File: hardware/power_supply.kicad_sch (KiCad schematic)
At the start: 45 parts

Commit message: schematic
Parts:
- removed C210, C?: (no value), symbol tinkerforge:CP1
- removed C? (x9): (no value), symbol tinkerforge:C
- removed D?: (no value), symbol tinkerforge:DIODESCH
- removed R? (x4): (no value), symbol tinkerforge:R
- removed U?: (no value), symbol tinkerforge:BD906XX-C-HRP7
- added C?: 100nF, kicad-libraries:C0603F, symbol tinkerforge:C
- added C? (x2): 47uF, kicad-libraries:C1210, symbol tinkerforge:C
- added C? (x2): 10uF, kicad-libraries:C0805E, symbol tinkerforge:C
- added R? (x2): 10k, kicad-libraries:R0603F, symbol tinkerforge:Rs
- added R?: 2k4, kicad-libraries:R0603F, symbol tinkerforge:Rs
- added U?: RPX-4.0, kicad-libraries:RPX-4.0, symbol tinkerforge:RPX-4.0
- C201: value (none) -> 100nF/16V; footprint (none) -> kicad-libraries:C0603F
- C203, C214: renamed from C?; value (none) -> 10uF/50V; footprint (none) -> kicad-libraries:C1210
- C215, C216: renamed from C?; value (none) -> 10uF; footprint (none) -> C1206
- C224: value (none) -> 470µF/16V; footprint (none) -> kicad-libraries:ELKO_83
- C225, C226: value (none) -> 1µF/10V; footprint (none) -> kicad-libraries:C0603F
- D202: value (none) -> Z12V; footprint (none) -> SOD-123
- J201: value (none) -> USB-C; footprint (none) -> kicad-libraries:USB-C
- L201, L202, L203: renamed from L?; value (none) -> 2.2uH 0530CDMCCDS-2R2MC; footprint (none) -> kicad-libraries:NRS5030
- P201: value (none) -> Black; footprint (none) -> kicad-libraries:OQ_2P
- Q201: value (none) -> SSM3J355R,LF; footprint (none) -> SOT23GDS
- Q202: value (none) -> Si4447ADY; footprint (none) -> kicad-libraries:SOIC-8-MOSFET
- R202, R203, R204, R207, R211: value (none) -> 10k; footprint (none) -> kicad-libraries:R0603F
- R205: value (none) -> 1k; footprint (none) -> kicad-libraries:R0603F
- R208: value (none) -> 47k; footprint (none) -> kicad-libraries:R0603F
- R212, R213: value (none) -> 5k1; footprint (none) -> kicad-libraries:R0603F
- R218: value (none) -> VC120626D580DP; footprint (none) -> R1206
- U202: value (none) -> DMMT5401; footprint (none) -> SOT26
- U205: value (none) -> AP7333-33SAG-7; footprint (none) -> kicad-libraries:SOT23-3
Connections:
- net 5VF: now also C?.1, C?.1, C?.1
- net GND: now also C?.2, C?.2, C?.2, C?.2, C?.2, R?.2, U?.10 (PGND), U?.11 (PGND), U?.12 (AGND), U?.15 (PGND), U?.3 (PGND)
- net VIN2: now also U?.1 (+Vin), U?.14 (+Vin), U?.2 (CTRL)
- net VSW: now also C?.1, C?.1, R?.1, U?.7 (Vout), U?.8 (Vout)
- new net: R?.2, U?.13 (PGS)
- new net: R?.1, R?.2, U?.9 (FB)
- new net PowerGood: R?.1, U?.6 (PG)
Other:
- note added: "max 36V"
- note removed: "max 28V"
- moved on the sheet: L201

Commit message: Proto V1.8
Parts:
- removed C215, C216: 10uF, C1206, symbol tinkerforge:C
- removed L203: 2.2uH 0530CDMCCDS-2R2MC, kicad-libraries:NRS5030, symbol tinkerforge:INDUCTOR
- added C6: 10uF/50V, kicad-libraries:C1210, symbol tinkerforge:C
- gave numbers to parts that had none: 9
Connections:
- net +5V: now also C3.1, C4.1, C5.1, L201.2
- net 3V3: now also R1.2
- net GND: now also C6.2
- net VIN2: now also C6.1
- net VSW: now also Q201.S, U202.5
- net at U1.13 (PGS): no longer R1.2
- removed net 5VF: C3.1, C4.1, C5.1, L201.2, Q201.S, U202.5
- no-connect marks 2 -> 3
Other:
- moved on the sheet: C201, C203, C224, C225, C226, C3, C4, C5, J201, Q201, R202, R203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

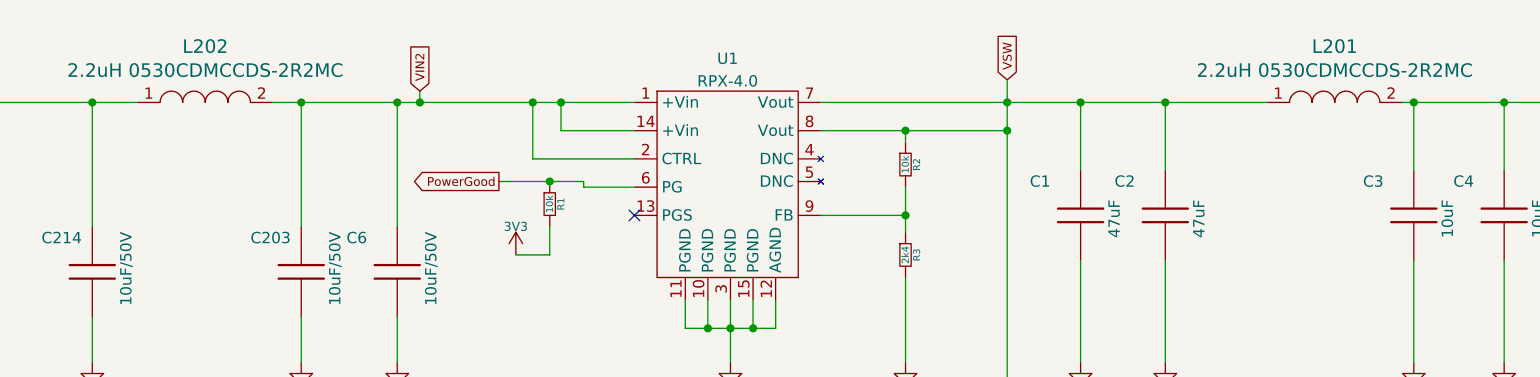
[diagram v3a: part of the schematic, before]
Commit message: move to kicad 7
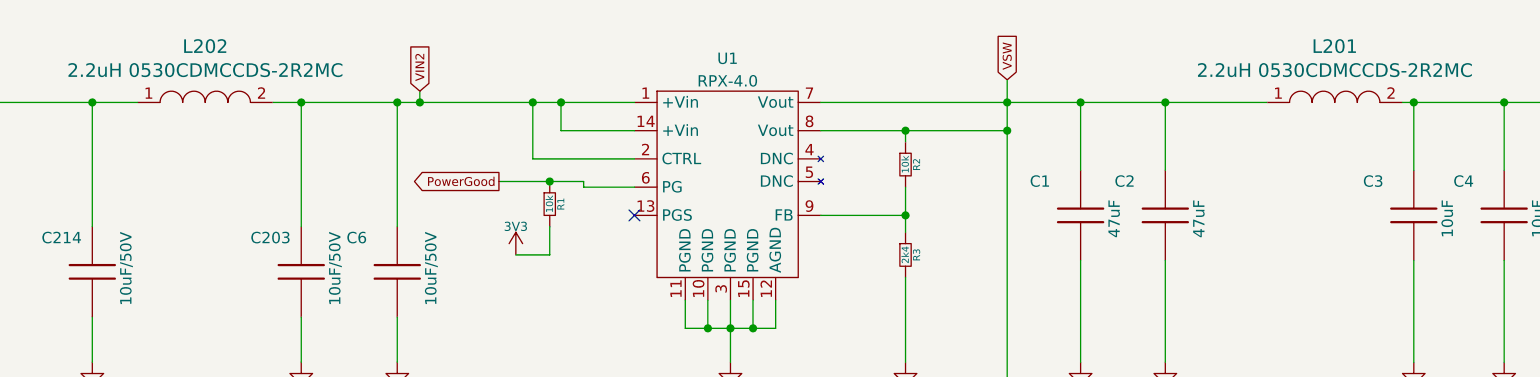
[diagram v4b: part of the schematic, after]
